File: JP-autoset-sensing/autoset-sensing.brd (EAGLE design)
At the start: 33.3 x 21.6 mm, 33 parts, among them J1 TERM_1X4_0.1, U2 LM293DT, U3 QRE1113GR, U4 QRE1113GR

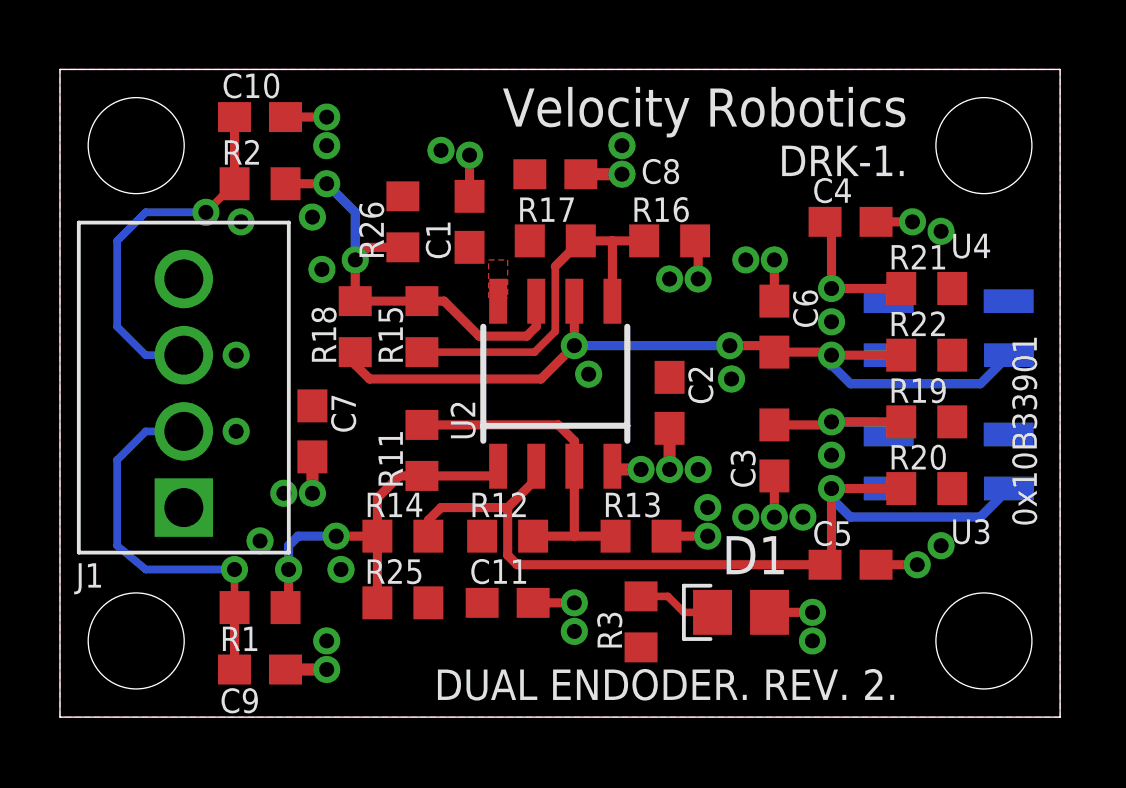
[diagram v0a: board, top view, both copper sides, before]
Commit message: Bord updates to go to 4 layers
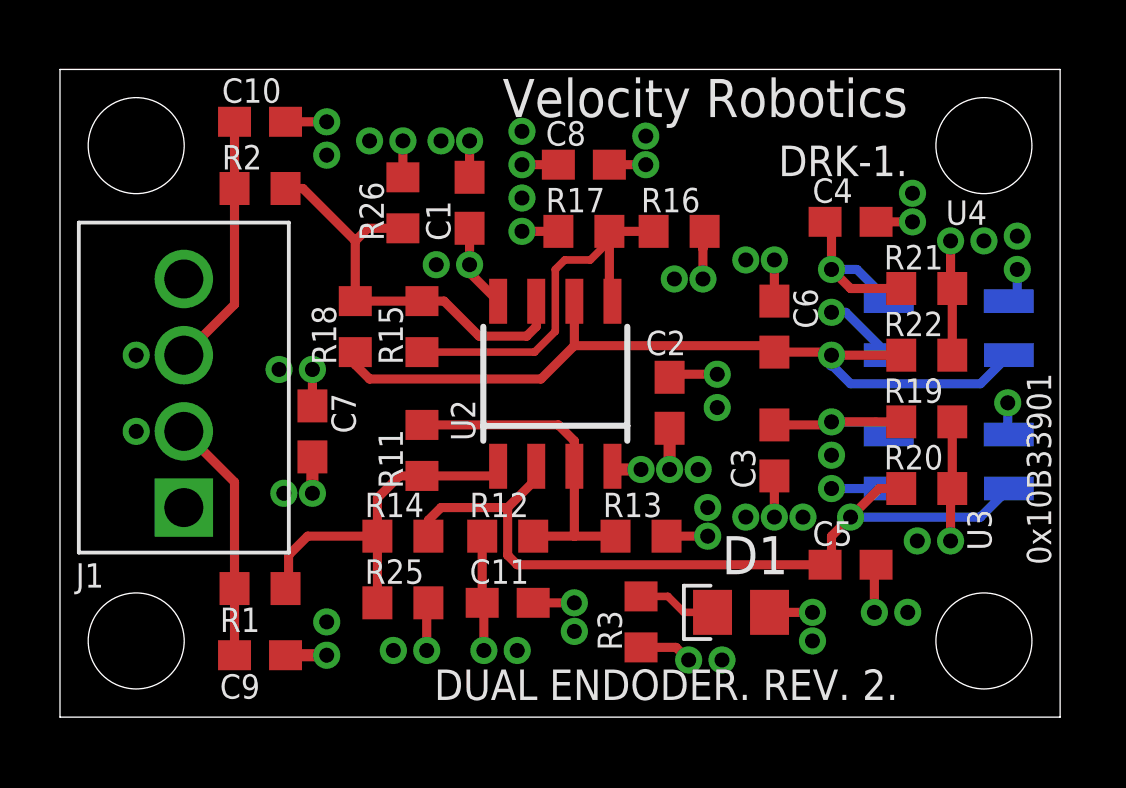
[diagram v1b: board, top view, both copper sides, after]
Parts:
- moved C8 1.00 mm to (17.5, 18.4)
- moved R17 1.00 mm to (17.5, 16.2)
- moved R1 0.63 mm to (6.67, 4.29)
- moved C1 0.63 mm to (13.7, 17.1)
- moved R26 0.63 mm to (11.4, 17.1)
- moved C9 0.48 mm to (6.67, 2.06)
- moved R16 0.45 mm to (20.6, 16.2)
- moved C10 0.16 mm to (6.67, 19.8)
- moved R2 0.16 mm to (6.67, 17.6)
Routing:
- net VDD: track 0.00 -> 24.3 mm, vias 0 -> 11
- net GND: track 19.9 -> 26.8 mm, vias 41 -> 49
- net N$1: track 13.0 -> 8.16 mm, vias 1 -> 0
- net N$2: track 12.4 -> 8.48 mm, vias 1 -> 0
- net VRING1: track 29.3 -> 27.1 mm
- net N$13: track 12.2 -> 13.2 mm
- net N$14: track 14.9 -> 14.3 mm, vias 2 -> 0
- net N$10: track 13.9 -> 13.8 mm, vias 2 -> 0
- net VRING2: vias 3 -> 1
- added copper zone on layer 2, net GND
- added copper zone on layer 15, net VDD
- removed copper zone on layer 16, net GND
- removed copper zone on layer 1, net VDD

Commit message: Multiple updates
Library update (add switch)
Updated sensing board to 4 layers, added some filtering.
Updated control board to 4 layers, added functionality.
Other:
- board text added: "0x10C33900"
- board text added: "DUAL ENDODER. REV. 3."
- board text removed: "0x10B33901"
- board text removed: "DUAL ENDODER. REV. 2."
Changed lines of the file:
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@@
 <hole x="2.54" y="19.05" drill="3.2"/>
 <text x="28.2575" y="21.2725" size="1.27" layer="21" font="vector" rot="R180">Velocity Robotics</text>
-<text x="27.94" y="1.5875" size="1.016" layer="21" font="vector" rot="R180">DUAL ENDODER. REV. 2.</text>
-<text x="32.22625" y="5.08" size="0.8128" layer="21" font="vector" rot="R270" align="bottom-right">0x10B33901</text>
+<text x="27.94" y="1.5875" size="1.016" layer="21" font="vector" rot="R180">DUAL ENDODER. REV. 3.</text>
+<text x="32.22625" y="5.08" size="0.8128" layer="21" font="vector" rot="R270" align="bottom-right">0x10C33900</text>
 <text x="28.2575" y="19.05" size="1.016" layer="21" font="vector" rot="R180">DRK-1.</text>
 <hole x="2.54" y="2.54" drill="3.2"/>
